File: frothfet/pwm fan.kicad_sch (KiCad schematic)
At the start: 6 parts, among them M1 Fan_Tacho, Q9 AO3400A

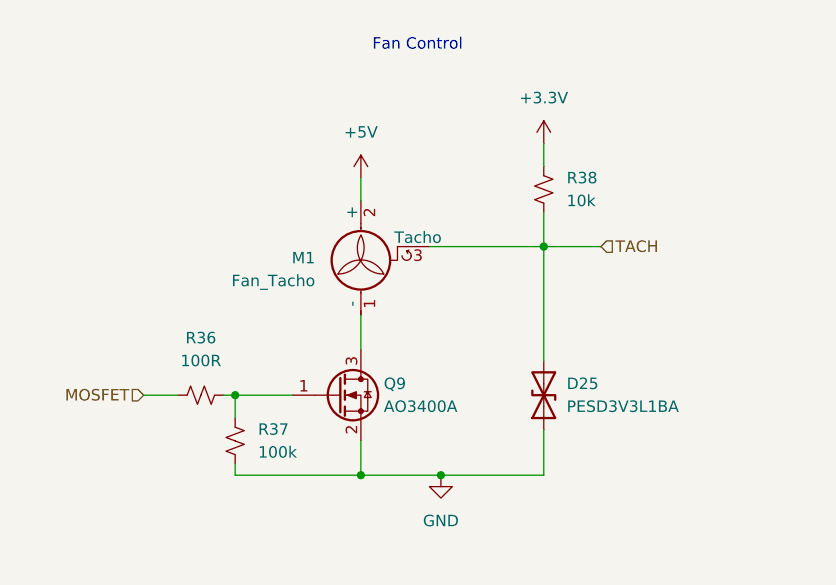
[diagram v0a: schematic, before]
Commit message: channel routing is basically done
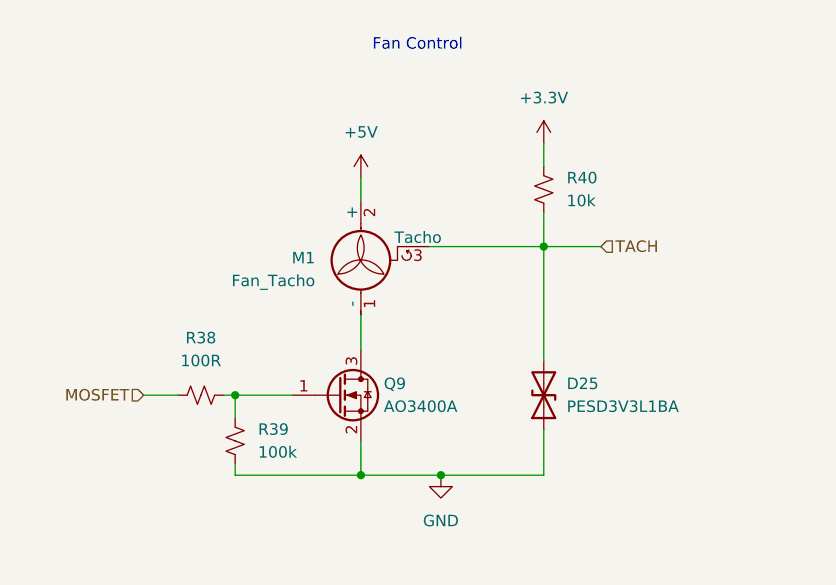
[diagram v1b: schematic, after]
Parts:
- renumbered R36 to R38, R37 to R39, R38 to R40
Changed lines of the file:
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@@
 		(dnp no)
 		(fields_autoplaced yes)
-		(property "Reference" "R38"
+		(property "Reference" "R40"
 			(at 156.21 72.39 0)
 			(effects
@@
 			(project "frothfet"
 				(path "/c83c6236-96e9-46ad-9d7a-9e2efa4a7966/02f6e629-b0e2-41e8-b2e4-f0e125a92a71"
-					(reference "R41")
-					(unit 1)
-				)
-				(path "/c83c6236-96e9-46ad-9d7a-9e2efa4a7966/ad82ad0c-2ba8-4934-bb2a-ed6e11658eb2"
-					(reference "R38")
+					(reference "R43")
+					(unit 1)
+				)
+				(path "/c83c6236-96e9-46ad-9d7a-9e2efa4a7966/ad82ad0c-2ba8-4934-bb2a-ed6e11658eb2"
+					(reference "R40")
 					(unit 1)
 				)
@@
 		(dnp no)
 		(fields_autoplaced yes)
-		(property "Reference" "R37"
+		(property "Reference" "R39"
 			(at 121.92 100.3299 0)
 			(effects
@@
 			(project "frothfet"
 				(path "/c83c6236-96e9-46ad-9d7a-9e2efa4a7966/02f6e629-b0e2-41e8-b2e4-f0e125a92a71"
-					(reference "R40")
-					(unit 1)
-				)
-				(path "/c83c6236-96e9-46ad-9d7a-9e2efa4a7966/ad82ad0c-2ba8-4934-bb2a-ed6e11658eb2"
-					(reference "R37")
+					(reference "R42")
+					(unit 1)
+				)
+				(path "/c83c6236-96e9-46ad-9d7a-9e2efa4a7966/ad82ad0c-2ba8-4934-bb2a-ed6e11658eb2"
+					(reference "R39")
 					(unit 1)
 				)
@@
 		(dnp no)
 		(fields_autoplaced yes)
-		(property "Reference" "R36"
+		(property "Reference" "R38"
 			(at 115.57 90.17 90)
 			(effects
@@
 			(project "8ch-mosfet"
 				(path "/c83c6236-96e9-46ad-9d7a-9e2efa4a7966/02f6e629-b0e2-41e8-b2e4-f0e125a92a71"
-					(reference "R39")
-					(unit 1)
-				)
-				(path "/c83c6236-96e9-46ad-9d7a-9e2efa4a7966/ad82ad0c-2ba8-4934-bb2a-ed6e11658eb2"
-					(reference "R36")
-					(unit 1)
-				)
+					(reference "R41")
+					(unit 1)
+				)
+				(path "/c83c6236-96e9-46ad-9d7a-9e2efa4a7966/ad82ad0c-2ba8-4934-bb2a-ed6e11658eb2"
+					(reference "R38")
+					(unit 1)
+				)

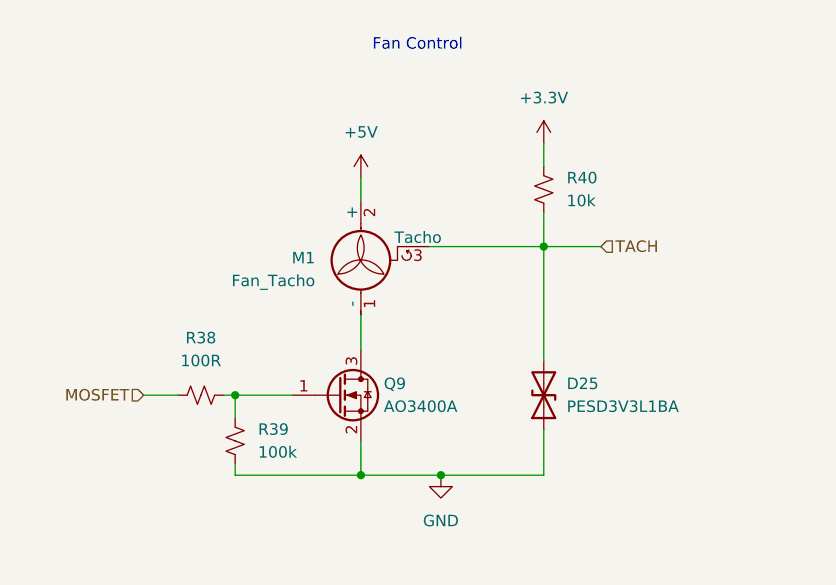
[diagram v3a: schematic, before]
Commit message: added support for ALERT pin from INA226 for overcurrent protection (hopefully)
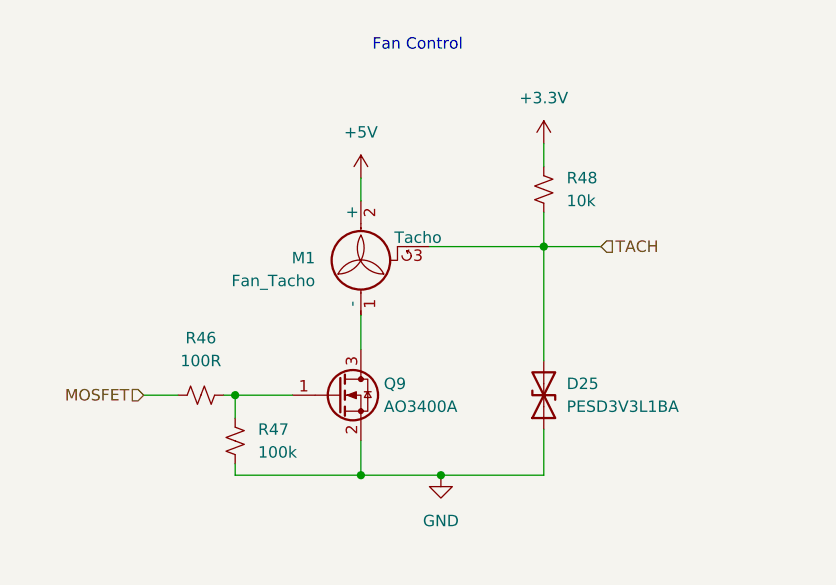
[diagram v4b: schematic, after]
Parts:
- renumbered R38 to R46, R39 to R47, R40 to R48
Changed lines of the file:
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@@
 		(dnp no)
 		(fields_autoplaced yes)
-		(property "Reference" "R40"
+		(property "Reference" "R48"
 			(at 156.21 72.39 0)
 			(effects
@@
 			(project "frothfet"
 				(path "/c83c6236-96e9-46ad-9d7a-9e2efa4a7966/02f6e629-b0e2-41e8-b2e4-f0e125a92a71"
-					(reference "R43")
-					(unit 1)
-				)
-				(path "/c83c6236-96e9-46ad-9d7a-9e2efa4a7966/ad82ad0c-2ba8-4934-bb2a-ed6e11658eb2"
-					(reference "R40")
+					(reference "R51")
+					(unit 1)
+				)
+				(path "/c83c6236-96e9-46ad-9d7a-9e2efa4a7966/ad82ad0c-2ba8-4934-bb2a-ed6e11658eb2"
+					(reference "R48")
 					(unit 1)
 				)
@@
 		(dnp no)
 		(fields_autoplaced yes)
-		(property "Reference" "R39"
+		(property "Reference" "R47"
 			(at 121.92 100.3299 0)
 			(effects
@@
 			(project "frothfet"
 				(path "/c83c6236-96e9-46ad-9d7a-9e2efa4a7966/02f6e629-b0e2-41e8-b2e4-f0e125a92a71"
-					(reference "R42")
-					(unit 1)
-				)
-				(path "/c83c6236-96e9-46ad-9d7a-9e2efa4a7966/ad82ad0c-2ba8-4934-bb2a-ed6e11658eb2"
-					(reference "R39")
+					(reference "R50")
+					(unit 1)
+				)
+				(path "/c83c6236-96e9-46ad-9d7a-9e2efa4a7966/ad82ad0c-2ba8-4934-bb2a-ed6e11658eb2"
+					(reference "R47")
 					(unit 1)
 				)
@@
 		(dnp no)
 		(fields_autoplaced yes)
-		(property "Reference" "R38"
+		(property "Reference" "R46"
 			(at 115.57 90.17 90)
 			(effects
@@
 			(project "8ch-mosfet"
 				(path "/c83c6236-96e9-46ad-9d7a-9e2efa4a7966/02f6e629-b0e2-41e8-b2e4-f0e125a92a71"
-					(reference "R41")
-					(unit 1)
-				)
-				(path "/c83c6236-96e9-46ad-9d7a-9e2efa4a7966/ad82ad0c-2ba8-4934-bb2a-ed6e11658eb2"
-					(reference "R38")
-					(unit 1)
-				)
+					(reference "R49")
+					(unit 1)
+				)
+				(path "/c83c6236-96e9-46ad-9d7a-9e2efa4a7966/ad82ad0c-2ba8-4934-bb2a-ed6e11658eb2"
+					(reference "R46")
+					(unit 1)
+				)

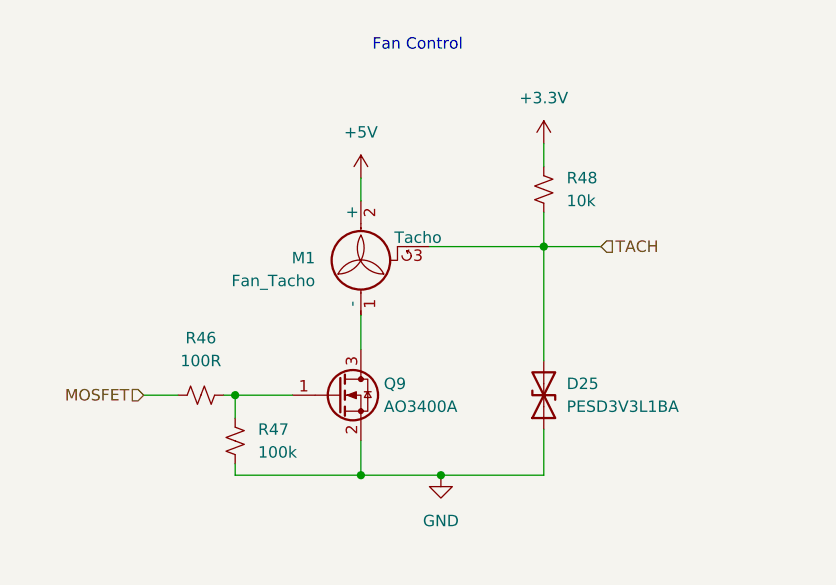
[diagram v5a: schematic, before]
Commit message: add esd protection to each channel output
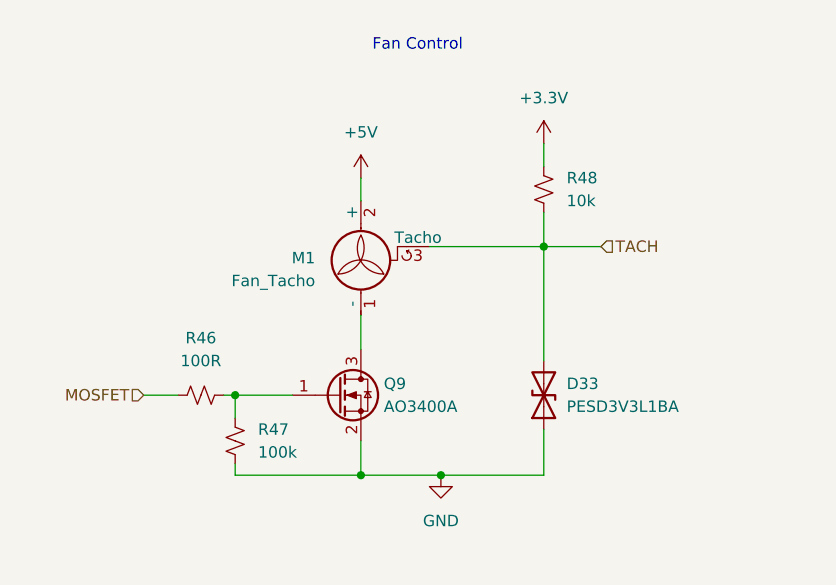
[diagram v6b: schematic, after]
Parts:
- renumbered D25 to D33
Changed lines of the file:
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@@
 		(on_board yes)
 		(dnp no)
-		(property "Reference" "D25"
+		(property "Reference" "D33"
 			(at 156.21 95.25 90)
 			(effects
@@
 			(project "frothfet"
 				(path "/c83c6236-96e9-46ad-9d7a-9e2efa4a7966/02f6e629-b0e2-41e8-b2e4-f0e125a92a71"
-					(reference "D26")
+					(reference "D34")
 					(unit 1)
 				)
 				(path "/c83c6236-96e9-46ad-9d7a-9e2efa4a7966/ad82ad0c-2ba8-4934-bb2a-ed6e11658eb2"
-					(reference "D25")
+					(reference "D33")
 					(unit 1)
 				)

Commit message: updated bom and checked placement
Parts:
- R46: LCSC (none) -> C22775
- R47: LCSC (none) -> C25803
- R48: LCSC (none) -> C25804
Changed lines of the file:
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@@
 			)
 		)
-		(property "LCSC" ""
+		(property "LCSC" "C25804"
 			(at 153.67 73.66 0)
 			(effects
@@
 			)
 		)
+		(property "LCSC" "C25803"
+			(at 119.38 101.6 0)
+			(effects
+				(font
+					(size 1.27 1.27)
+				)
+				(hide yes)
+			)
+		)
 		(pin "1"
 		)
@@
 			)
 		)
-		(property "LCSC" ""
+		(property "LCSC" "C22775"
 			(at 115.57 96.52 0)
 			(effects

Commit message: finished vias, added a bunch of test points
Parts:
- added TP89: TestPoint, TestPoint:TestPoint_Pad_D1.5mm, symbol Connector:TestPoint
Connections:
- net TACH: now also TP89.1
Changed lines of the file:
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@@
 		(company "https://github.com/hoeken/frothfet")
+	)
+	(rectangle
+		(start 95.25 54.61)
+		(end 184.15 115.57)
+		(stroke
+			(width 0)
+			(type default)
+		)
+		(fill
+			(type none)
+		)
 	)
 	(text "Fan Control"
 		(exclude_from_sim no)
-		(at 134.62 58.42 0)
+		(at 96.52 58.42 0)
 		(effects
 			(font
-				(size 1.27 1.27)
+				(size 2 2)
+				(thickness 0.4)
+				(bold yes)
 			)
 			(justify left bottom)
@@
 		(color 0 0 0 0)
 	)
+	(junction
+		(at 160.02 80.01)
+		(diameter 0)
+		(color 0 0 0 0)
+	)
 	(wire
 		(pts
@@
 	(wire
 		(pts
+			(xy 160.02 80.01) (xy 165.1 80.01)
+		)
+		(stroke
+			(width 0)
+			(type default)
+		)
+	)
+	(wire
+		(pts
 			(xy 118.11 96.52) (xy 119.38 96.52)
 		)
@@
 	(wire
 		(pts
-			(xy 133.35 72.39) (xy 133.35 74.93)
+			(xy 133.35 68.58) (xy 133.35 74.93)
 		)
 		(stroke
@@
 	(hierarchical_label "TACH"
 		(shape input)
-		(at 160.02 80.01 0)
+		(at 165.1 80.01 0)
 		(effects
 			(font
@@
 				(path "/c83c6236-96e9-46ad-9d7a-9e2efa4a7966/ad82ad0c-2ba8-4934-bb2a-ed6e11658eb2"
 					(reference "D33")
+					(unit 1)
+				)
+			)
+		)
+	)
+	(symbol
+		(lib_id "Connector:TestPoint")
+		(at 160.02 80.01 0)
+		(mirror x)
+		(unit 1)
+		(exclude_from_sim no)
+		(in_bom yes)
+		(on_board yes)
+		(dnp no)
+		(property "Reference" "TP89"
+			(at 158.75 85.09 0)
+			(effects
+				(font
+					(size 1.27 1.27)
+				)
+				(justify left)
+			)
+		)
+		(property "Value" "TestPoint"
+			(at 162.56 82.0421 0)
+			(effects
+				(font
+					(size 1.27 1.27)
+				)
+				(justify left)
+				(hide yes)
+			)
+		)
+		(property "Footprint" "TestPoint:TestPoint_Pad_D1.5mm"
+			(at 165.1 80.01 0)
+			(effects
+				(font
+					(size 1.27 1.27)
+				)
+				(hide yes)
+			)
+		)
+		(property "Datasheet" "~"
+			(at 165.1 80.01 0)
+			(effects
+				(font
+					(size 1.27 1.27)
+				)
+				(hide yes)
+			)
+		)
+		(property "Description" "test point"
+			(at 160.02 80.01 0)
+			(effects
+				(font
+					(size 1.27 1.27)
+				)
+				(hide yes)
+			)
+		)
+		(pin "1"
+		)
+		(instances
+			(project "frothfet"
+				(path "/c83c6236-96e9-46ad-9d7a-9e2efa4a7966/02f6e629-b0e2-41e8-b2e4-f0e125a92a71"
+					(reference "TP90")
+					(unit 1)
+				)
+				(path "/c83c6236-96e9-46ad-9d7a-9e2efa4a7966/ad82ad0c-2ba8-4934-bb2a-ed6e11658eb2"
+					(reference "TP89")
 					(unit 1)
 				)
@@
 	(symbol
 		(lib_id "power:+5V")
-		(at 133.35 72.39 0)
+		(at 133.35 68.58 0)
 		(unit 1)
 		(exclude_from_sim no)
@@
 		(fields_autoplaced yes)
 		(property "Reference" "#PWR0125"
-			(at 133.35 76.2 0)
+			(at 133.35 72.39 0)
 			(effects
 				(font
@@
 		)
 		(property "Value" "+5V"
-			(at 133.35 67.31 0)
+			(at 133.35 63.5 0)
 			(effects
 				(font
@@
 		)
 		(property "Footprint" ""
-			(at 133.35 72.39 0)
+			(at 133.35 68.58 0)
 			(effects
 				(font
@@
 		)
 		(property "Datasheet" ""
-			(at 133.35 72.39 0)
+			(at 133.35 68.58 0)
 			(effects
 				(font
@@
 		)
 		(property "Description" "Power symbol creates a global label with name \"+5V\""
-			(at 133.35 72.39 0)
-			(effects
-				(font
+			(at 133.35 68.58 0)
+			(effects
+				(font
